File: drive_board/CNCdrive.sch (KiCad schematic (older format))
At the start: 40 parts, among them P1 CONN_01X14, P2 CONN_01X04, Q1 Q_NMOS_GDS, Q2 Q_NMOS_GDS, Q3 Q_NMOS_GDS, Q4 Q_NMOS_GDS, Q5 Q_NMOS_GDS, Q6 Q_NMOS_GDS, Q7 Q_NMOS_GDS, Q8 Q_NMOS_GDS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

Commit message: new GND for digital
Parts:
- added P?: CONN_01X02, symbol CONN_01X02
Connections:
- net +48V: now also P?.1 (P1)
- net GND: now also P?.2 (P2); no longer C1.2, C2.2, C3.2, C4.2, C8.2, D1.1 (K), D2.1 (K), P1.14 (P14), U1.29 (GND), U1.38 (GND), U1.5 (GND)
- net BEMF: now reaches C8.1, U1.20 (BEMF)
- net BEMF: now also P1.13 (P13)
- new net GNDD: C1.2, C2.2, C3.2, C4.2, C8.2, D1.1 (K), D2.1 (K), P1.14 (P14), U1.29 (GND), U1.38 (GND), U1.5 (GND)
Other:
- note added: "+protection diodes to D-S?\n"
- note removed: "+protection diodes to G-S?\n"
- note removed: "are series resistors required? other termination?"
- note removed: "might cause higher dissipation in drv8711\n"
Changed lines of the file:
@@
-$EndComp
-$Comp
-L GND #PWR02
-U 1 1 56D082D5
-P 2600 2700
-F 0 "#PWR02" H 2600 2450 50  0001 C CNN
-F 1 "GND" H 2600 2550 50  0000 C CNN
-F 2 "" H 2600 2700 50  0000 C CNN
-F 3 "" H 2600 2700 50  0000 C CNN
-	1    2600 2700
-	1    0    0    -1
 $EndComp
 $Comp
@@
 $EndComp
 $Comp
-L GND #PWR06
-U 1 1 56D0F74B
-P 7500 4200
-F 0 "#PWR06" H 7500 3950 50  0001 C CNN
-F 1 "GND" H 7500 4050 50  0000 C CNN
-F 2 "" H 7500 4200 50  0000 C CNN
-F 3 "" H 7500 4200 50  0000 C CNN
-	1    7500 4200
-	1    0    0    -1
-$EndComp
-$Comp
 L Q_NMOS_GDS Q2
 U 1 1 56D0B718
@@
 F 3 "" H 9750 3300 50  0000 C CNN
 	1    9750 3300
-	1    0    0    -1
-$EndComp
-$Comp
-L GND #PWR010
-U 1 1 56D0F90E
-P 7400 1800
-F 0 "#PWR010" H 7400 1550 50  0001 C CNN
-F 1 "GND" H 7400 1650 50  0000 C CNN
-F 2 "" H 7400 1800 50  0000 C CNN
-F 3 "" H 7400 1800 50  0000 C CNN
-	1    7400 1800
-	1    0    0    -1
-$EndComp
-$Comp
-L GND #PWR011
-U 1 1 56D11F1F
-P 8650 2950
-F 0 "#PWR011" H 8650 2700 50  0001 C CNN
-F 1 "GND" H 8650 2800 50  0000 C CNN
-F 2 "" H 8650 2950 50  0000 C CNN
-F 3 "" H 8650 2950 50  0000 C CNN
-	1    8650 2950
 	1    0    0    -1
 $EndComp
@@
 Text HLabel 10350 6100 2    60   Input ~ 0
 BISENN
-Text Notes 4050 3700 2    60   ~ 0
-are series resistors required? other termination?
-Text HLabel 3900 3300 0    60   Input ~ 0
+Text HLabel 5100 3300 0    60   Input ~ 0
 SCLK
-Text HLabel 3900 3400 0    60   Input ~ 0
+Text HLabel 5100 3400 0    60   Input ~ 0
 SDATI
-Text HLabel 3900 3500 0    60   Input ~ 0
+Text HLabel 5100 3500 0    60   Input ~ 0
 SCS
-$Comp
-L GND #PWR015
-U 1 1 56D34EEC
-P 3600 2450
-F 0 "#PWR015" H 3600 2200 50  0001 C CNN
-F 1 "GND" H 3600 2300 50  0000 C CNN
-F 2 "" H 3600 2450 50  0000 C CNN
-F 3 "" H 3600 2450 50  0000 C CNN
-	1    3600 2450
-	1    0    0    -1
-$EndComp
-Text HLabel 3900 3200 0    60   Input ~ 0
+Text HLabel 5100 3200 0    60   Input ~ 0
 BIN2
-Text HLabel 3900 3100 0    60   Input ~ 0
+Text HLabel 5100 3100 0    60   Input ~ 0
 BIN1
-Text HLabel 3900 3000 0    60   Input ~ 0
+Text HLabel 5100 3000 0    60   Input ~ 0
 DIR/AIN2
-Text HLabel 3900 2900 0    60   Input ~ 0
+Text HLabel 5100 2900 0    60   Input ~ 0
 STEP/AIN1
-Text HLabel 3900 2800 0    60   Input ~ 0
+Text HLabel 5100 2800 0    60   Input ~ 0
 RESET
-Text HLabel 3900 2700 0    60   Input ~ 0
+Text HLabel 5100 2700 0    60   Input ~ 0
 ~SLEEP
 Text HLabel 1050 4400 2    60   Output ~ 0
@@
 	0    -1   -1   0
 $EndComp
-$Comp
-L GND #PWR018
-U 1 1 56D2DDF9
-P 2400 6400
-F 0 "#PWR018" H 2400 6150 50  0001 C CNN
-F 1 "GND" H 2400 6250 50  0000 C CNN
-F 2 "" H 2400 6400 50  0000 C CNN
-F 3 "" H 2400 6400 50  0000 C CNN
-	1    2400 6400
-	1    0    0    -1
-$EndComp
-$Comp
-L GND #PWR019
-U 1 1 56D2E266
-P 2800 6400
-F 0 "#PWR019" H 2800 6150 50  0001 C CNN
-F 1 "GND" H 2800 6250 50  0000 C CNN
-F 2 "" H 2800 6400 50  0000 C CNN
-F 3 "" H 2800 6400 50  0000 C CNN
-	1    2800 6400
-	1    0    0    -1
-$EndComp
-Text Notes 2900 6000 0    60   ~ 0
-might cause higher dissipation in drv8711\n
-Text Notes 5650 4600 0    60   ~ 0
+Text Notes 5550 4900 0    60   ~ 0
 should we put terminals for DC motors?
 Text Notes 5250 5200 0    60   ~ 0
@@
 	4550 4750 4550 3800
 Wire Wire Line
-	7500 3850 7500 3800
-Wire Wire Line
 	7500 4200 7500 4150
 Wire Wire Line
@@
 Connection ~ 9300 2650
 Wire Wire Line
-	7500 3800 7450 3800
+	7450 3800 7550 3800
 Wire Wire Line
 	5250 2100 5100 2100
@@
 	7950 3600 7450 3600
 Wire Wire Line
-	7450 3700 7800 3700
-Wire Wire Line
-	7800 3700 7800 6500
-Wire Wire Line
-	7800 6500 10800 6500
+	7450 3700 7850 3700
+Wire Wire Line
+	7850 3700 7850 6500
+Wire Wire Line
+	7850 6500 10800 6500
 Wire Wire Line
 	10800 6500 10800 5700
@@
 Connection ~ 10000 6350
 Wire Wire Line
-	3900 3500 5250 3500
-Wire Wire Line
-	3900 3400 5250 3400
+	5100 3500 5250 3500
+Wire Wire Line
+	5100 3400 5250 3400
 Wire Wire Line
 	3800 2400 3600 2400
@@
 Connection ~ 9300 1250
 Wire Wire Line
-	3900 3300 5250 3300
+	5100 3300 5250 3300
 Wire Wire Line
 	4450 3700 5250 3700
@@
 	4550 3800 5250 3800
 Wire Wire Line
-	3900 3200 5250 3200
-Wire Wire Line
-	3900 3100 5250 3100
-Wire Wire Line
-	3900 3000 5250 3000
-Wire Wire Line
-	3900 2900 5250 2900
-Wire Wire Line
-	3900 2800 5250 2800
-Wire Wire Line
-	3900 2700 5250 2700
+	5100 3200 5250 3200
+Wire Wire Line
+	5100 3100 5250 3100
+Wire Wire Line
+	5100 3000 5250 3000
+Wire Wire Line
+	5100 2900 5250 2900
+Wire Wire Line
+	5100 2800 5250 2800
+Wire Wire Line
+	5100 2700 5250 2700
 $Comp
 L CONN_01X14 P1
@@
 	-1   0    0    -1
 $EndComp
-$Comp
-L GND #PWR022
-U 1 1 56DBA966
+Wire Wire Line
+	1050 4600 1100 4600
+Wire Wire Line
+	1100 4600 1100 4650
+Text Notes 9900 1150 0    60   ~ 0
++protection diodes to D-S?\n
+$Comp
+L GNDD #PWR?
+U 1 1 56D8FE1C
+P 7500 4200
+F 0 "#PWR?" H 7500 3950 50  0001 C CNN
+F 1 "GNDD" H 7500 4050 50  0000 C CNN
+F 2 "" H 7500 4200 50  0000 C CNN
+F 3 "" H 7500 4200 50  0000 C CNN
+	1    7500 4200
+	1    0    0    -1
+$EndComp
+$Comp
+L GNDD #PWR?
+U 1 1 56D91081
+P 7400 1800
+F 0 "#PWR?" H 7400 1550 50  0001 C CNN
+F 1 "GNDD" H 7400 1650 50  0000 C CNN
+F 2 "" H 7400 1800 50  0000 C CNN
+F 3 "" H 7400 1800 50  0000 C CNN
+	1    7400 1800
+	1    0    0    -1
+$EndComp
+$Comp
+L GNDD #PWR?
+U 1 1 56D931D6
+P 3600 2450
+F 0 "#PWR?" H 3600 2200 50  0001 C CNN
+F 1 "GNDD" H 3600 2300 50  0000 C CNN
+F 2 "" H 3600 2450 50  0000 C CNN
+F 3 "" H 3600 2450 50  0000 C CNN
+	1    3600 2450
+	1    0    0    -1
+$EndComp
+$Comp
+L GNDD #PWR?
+U 1 1 56D93259
+P 2600 2700
+F 0 "#PWR?" H 2600 2450 50  0001 C CNN
+F 1 "GNDD" H 2600 2550 50  0000 C CNN
+F 2 "" H 2600 2700 50  0000 C CNN
+F 3 "" H 2600 2700 50  0000 C CNN
+	1    2600 2700
+	1    0    0    -1
+$EndComp
+$Comp
+L GNDD #PWR?
+U 1 1 56D93518
 P 1100 4650
-F 0 "#PWR022" H 1100 4400 50  0001 C CNN
-F 1 "GND" H 1100 4500 50  0000 C CNN
+F 0 "#PWR?" H 1100 4400 50  0001 C CNN
+F 1 "GNDD" H 1100 4500 50  0000 C CNN
 F 2 "" H 1100 4650 50  0000 C CNN
 F 3 "" H 1100 4650 50  0000 C CNN
@@
 	1    0    0    -1
 $EndComp
-Wire Wire Line
-	1050 4600 1100 4600
-Wire Wire Line
-	1100 4600 1100 4650
-Text Notes 9900 1150 0    60   ~ 0
-+protection diodes to G-S?\n
+$Comp
+L GNDD #PWR?
+U 1 1 56D950B1
+P 2800 6400
+F 0 "#PWR?" H 2800 6150 50  0001 C CNN
+F 1 "GNDD" H 2800 6250 50  0000 C CNN
+F 2 "" H 2800 6400 50  0000 C CNN
+F 3 "" H 2800 6400 50  0000 C CNN
+	1    2800 6400
+	1    0    0    -1
+$EndComp
+$Comp
+L GNDD #PWR?
+U 1 1 56D95314
+P 2400 6400
+F 0 "#PWR?" H 2400 6150 50  0001 C CNN
+F 1 "GNDD" H 2400 6250 50  0000 C CNN
+F 2 "" H 2400 6400 50  0000 C CNN
+F 3 "" H 2400 6400 50  0000 C CNN
+	1    2400 6400
+	1    0    0    -1
+$EndComp
+$Comp
+L GNDD #PWR?
+U 1 1 56D96B30
+P 8650 2950
+F 0 "#PWR?" H 8650 2700 50  0001 C CNN
+F 1 "GNDD" H 8650 2800 50  0000 C CNN
+F 2 "" H 8650 2950 50  0000 C CNN
+F 3 "" H 8650 2950 50  0000 C CNN
+	1    8650 2950
+	1    0    0    -1
+$EndComp
+Text HLabel 7550 3800 2    60   Output ~ 0
+BEMF
+Wire Wire Line
+	7500 3850 7500 3800
+Connection ~ 7500 3800
+Text HLabel 1050 4500 2    60   Output ~ 0
+BEMF
+$Comp
+L CONN_01X02 P?
+U 1 1 56DA2DCD
+P 1400 1500
+F 0 "P?" H 1400 1650 50  0000 C CNN
+F 1 "CONN_01X02" V 1500 1500 50  0000 C CNN
+F 2 "" H 1400 1500 50  0000 C CNN
+F 3 "" H 1400 1500 50  0000 C CNN
+	1    1400 1500
+	-1   0    0    -1
+$EndComp
+$Comp
+L +48V #PWR?
+U 1 1 56DA31ED
+P 5400 900
+F 0 "#PWR?" H 5400 750 50  0001 C CNN
+F 1 "+48V" H 5400 1040 50  0000 C CNN
+F 2 "" H 5400 900 50  0000 C CNN
+F 3 "" H 5400 900 50  0000 C CNN
+	1    5400 900
+	1    0    0    -1
+$EndComp
+$Comp
+L +48V #PWR?
+U 1 1 56DA32FB
+P 1650 1450
+F 0 "#PWR?" H 1650 1300 50  0001 C CNN
+F 1 "+48V" H 1650 1590 50  0000 C CNN
+F 2 "" H 1650 1450 50  0000 C CNN
+F 3 "" H 1650 1450 50  0000 C CNN
+	1    1650 1450
+	1    0    0    -1
+$EndComp
+$Comp
+L GND #PWR?
+U 1 1 56DA3C79
+P 1650 1550
+F 0 "#PWR?" H 1650 1300 50  0001 C CNN
+F 1 "GND" H 1650 1400 50  0000 C CNN
+F 2 "" H 1650 1550 50  0000 C CNN
+F 3 "" H 1650 1550 50  0000 C CNN
+	1    1650 1550
+	1    0    0    -1
+$EndComp
+Wire Wire Line
+	1600 1550 1650 1550
+Wire Wire Line
+	1600 1450 1650 1450
 $EndSCHEMATC

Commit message: drive board done
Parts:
- added D? (x8): D_Schottky, symbol D_Schottky
- added F?: 5A, symbol FUSE
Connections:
- net +48V: now also D?.1 (K), D?.1 (K), D?.1 (K), D?.1 (K), F?.2; no longer P?.1 (P1)
- net AISENP: now also D?.2 (A), D?.2 (A)
- net BISENP: now also D?.2 (A), D?.2 (A)
- net at D9.2 (A), P2.4 (P4), Q7.3 (S)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: now also D?.1 (K), D?.2 (A)
- net at D7.2 (A), P2.3 (P3), Q5.3 (S)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: now also D?.1 (K), D?.2 (A)
- net at D5.2 (A), P2.2 (P2), Q3.3 (S)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: now also D?.1 (K), D?.2 (A)
- net at D3.2 (A), P2.1 (P1), Q1.3 (S)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: now also D?.1 (K), D?.2 (A)
- new net: F?.1, P?.1 (P1)
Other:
- note removed: "+protection diodes to D-S?\n"
- note removed: "bulk capacitor (bank?) for Vmot is needed"
- note removed: "optional RC filter on xISENy inputs? datasheet p18"
- note removed: "should we put terminals for DC motors?"

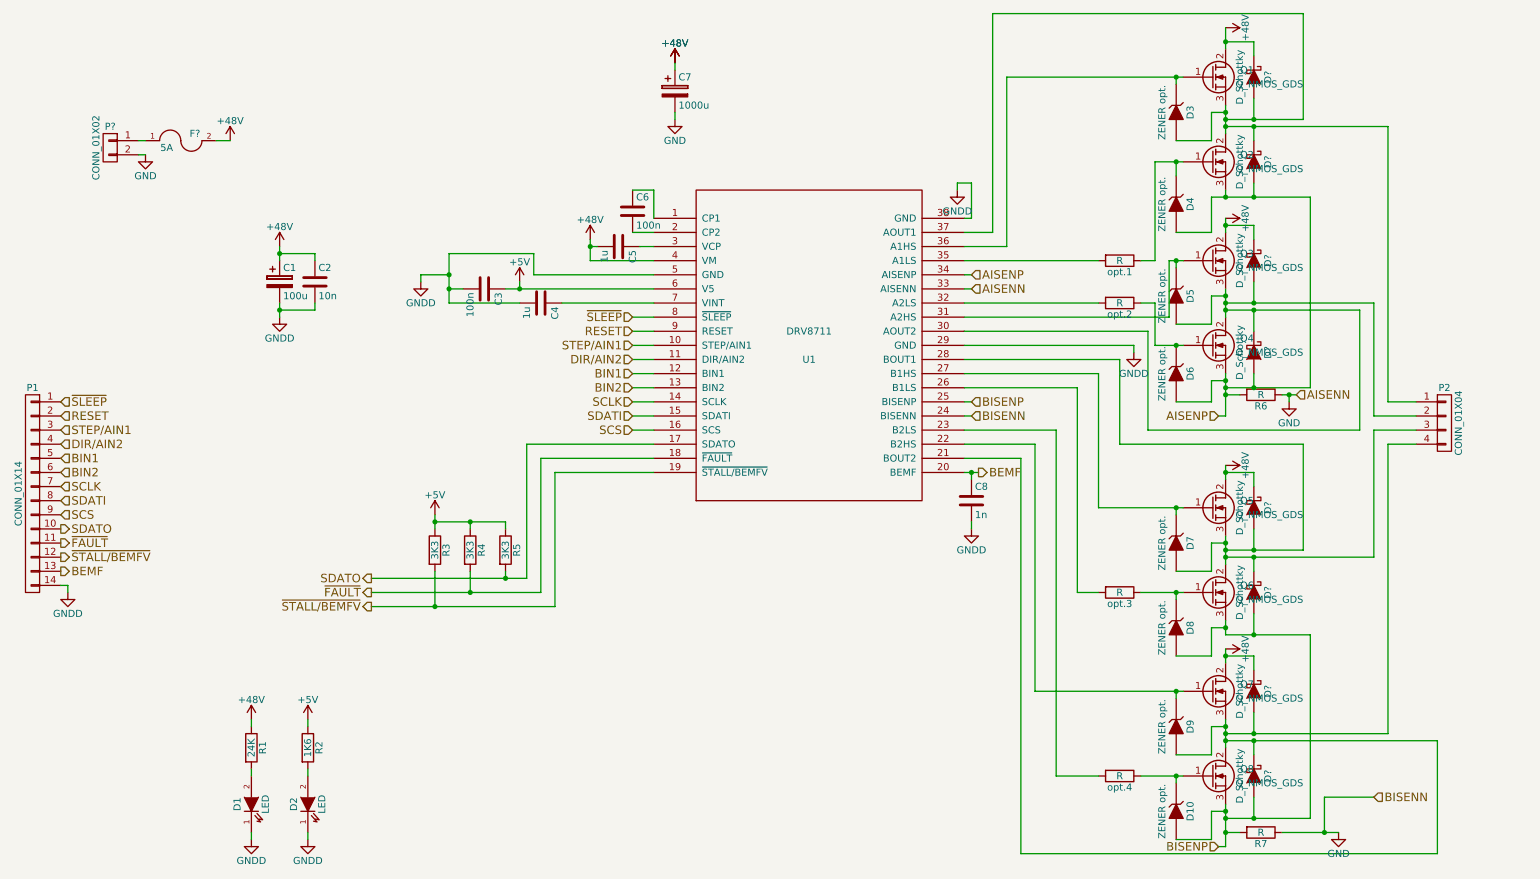
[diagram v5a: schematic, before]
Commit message: added snubber, drive board is 100% done
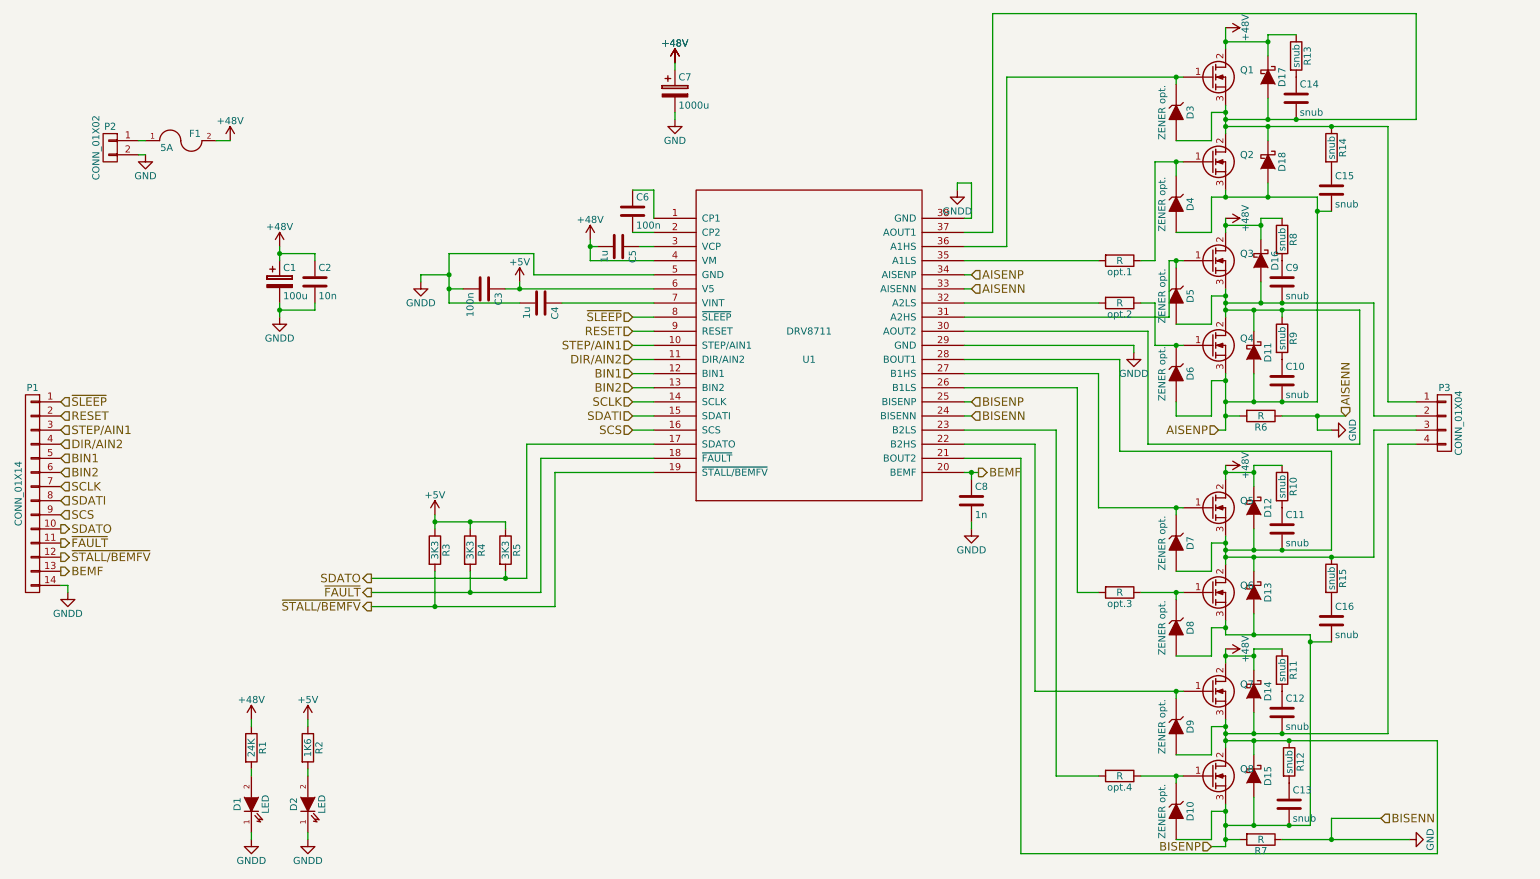
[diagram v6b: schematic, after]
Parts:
- added C10, C11, C12, C13, C14, C15, C16, C9: snub, symbol C
- added R10, R11, R12, R13, R14, R15, R8, R9: snub, symbol R
- gave numbers to parts that had none: 10
- renumbered P2 to P3
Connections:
- net +48V: now also R10.1, R11.1, R13.1, R8.1
- net AISENP: now also C10.2, C15.2
- net BISENP: now also C13.2, C16.2
- net at D14.2 (A), D15.1 (K), D9.2 (A)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: now also C12.2, R12.1
- net at D12.2 (A), D13.1 (K), D7.2 (A)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: now also C11.2, R15.1
- net at D11.1 (K), D16.2 (A), D5.2 (A)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: now also C9.2, R9.1
- net at D17.2 (A), D18.1 (K), D3.2 (A)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: now also C14.2, R14.1
- new net: C14.1, R13.2
- new net: C15.1, R14.2
- new net: C9.1, R8.2
- new net: C10.1, R9.2
- new net: C11.1, R10.2
- new net: C16.1, R15.2
- new net: C13.1, R12.2
- new net: C12.1, R11.2
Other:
- moved on the sheet: D16, D17, D18, R6, R7

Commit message: associated footprints, connectors, fuse, leds might need change
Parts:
- C1, C2, C3, C4, C5, C6, C8: footprint (none) -> Capacitors_SMD:C_1206_HandSoldering
- C10, C11, C12, C13, C14, C15, C16, C9: footprint (none) -> Capacitors_SMD:C_0805_HandSoldering
- C7: footprint (none) -> Capacitors_ThroughHole:C_Radial_D22_L41_P10
- D1, D2: footprint (none) -> LEDs:LED_1206
- D10, D11, D12, D13, D14, D15, D16, D17, D18, D3, D4, D5, D6, D7, D8, D9: footprint (none) -> Diodes_SMD:SOD-123
- F1: footprint (none) -> Fuse_Holders_and_Fuses:Fuse_SMD1206_HandSoldering
- P1: footprint (none) -> Connectors_Molex:Connector_Molex_PicoBlade_53048-1410
- P2: footprint (none) -> Terminal_Blocks:TerminalBlock_Pheonix_PT-3.5mm_2pol
- P3: footprint (none) -> Terminal_Blocks:TerminalBlock_Pheonix_PT-3.5mm_4pol
- Q1, Q2, Q3, Q4, Q5, Q6, Q7, Q8: footprint (none) -> TO_SOT_Packages_THT:TO-220_Neutral123_Vertical_LargePads
- R1, R10, R11, R12, R13, R14, R15, R2, R3, R4, R5, R8, R9, opt.1, opt.2, opt.3, opt.4: footprint (none) -> Resistors_SMD:R_0805_HandSoldering
- R6, R7: footprint (none) -> Resistors_SMD:R_2512_HandSoldering
